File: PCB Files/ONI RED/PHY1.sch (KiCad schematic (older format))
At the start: 40 parts

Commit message: Continued routing work
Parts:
- removed C? (x14): 0.1uF, symbol Device:C_Small
- removed C?: 10uF, symbol Device:CP1_Small
- removed D? (x2): 1N4148, symbol Device:D
- removed J?: JK0654219, Connector_RJ:RJ45_Pulse_JK0654219NL_Horizontal, symbol Connector:JK0654219
- removed R?: 4.7K, symbol Device:R
- removed R? (x2): 10k, symbol Device:R_Small
- removed R?: 220, symbol Device:R_Small
- removed R? (x4): 4.7k, symbol Device:R_Small
- added C43: 10uF, symbol Device:CP1_Small
- added C44, C48, C50, C54, C55: 0.1uF, symbol Device:C_Small
- added C45, C51: 100nF, symbol Device:C_Small
- added C46, C49, C52, C57: 10uF, symbol Device:C_Small
- added C47, C53, C56: 1uF, symbol Device:C_Small
- added D3, D4: 1N4148, symbol Device:D
- added J2: JK0654219, Connector_RJ:RJ45_Pulse_JK0654219NL_Horizontal, symbol Connector:JK0654219
- added R29: 4.7K, symbol Device:R
- added R31, R32, R33, R34: 4.7k, symbol Device:R_Small
- added R35, R39: 10k, symbol Device:R_Small
- added R40: 220, symbol Device:R_Small
- gave numbers to parts that had none: 14
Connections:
- net +3.3V: now also C44.1, C45.1, C46.1, C47.1, C48.1, D4.1 (K), R29.1, R31.2, R32.2, R33.2, R34.1, R35.2, R39.1, R40.2
- net AVDDL: now also C55.1, C56.1, C57.1
- net CLK125: now also R29.2
- net DVDDL: now also C49.1, C50.1, C51.1, C52.1, C53.1, C54.1
- net GND: now also C43.2, C44.2, C45.2, C46.2, C47.2, C48.2, C49.2, C50.2, C51.2, C52.2, C53.2, C54.2, C55.2, C56.2, C57.2
- net M_A: now also J2.10 (MX1-)
- net M_B: now also J2.4 (MX2+)
- net M_C: now also J2.2 (MX3-)
- net M_D: now also J2.9 (MX4-)
- net PHYAD0: now also J2.15 (LED1-), R39.2
- net PHYAD1: now also J2.13 (LED2-)
- net P_A: now also J2.11 (MX1+)
- net P_B: now also J2.5 (MX2-)
- net P_C: now also J2.3 (MX3+)
- net P_D: now also J2.8 (MX4+)
- net RXD1: now also R31.1
- net RXD2: now also R32.1
- net RX_DV: now also R34.2
- net at U9.42 (RESET_N): now also C43.1, D3.2 (A), D4.2 (A), R35.1
- net at C62.1: now also J2.1 (MXCT3)
- net at C60.1: now also J2.12 (MXCT1)
- net at R42.2: now also J2.16 (LED1+)
- net at C61.1: now also J2.6 (MXCT2)
- net at C63.1: now also J2.7 (MXCT4)
- net RX23 renamed RXD3
- net RXD3: now also R33.1
- net TXDO renamed TXD0
- new net: J2.14 (LED2+), R40.1
- new net RESET_N: D3.1 (K)

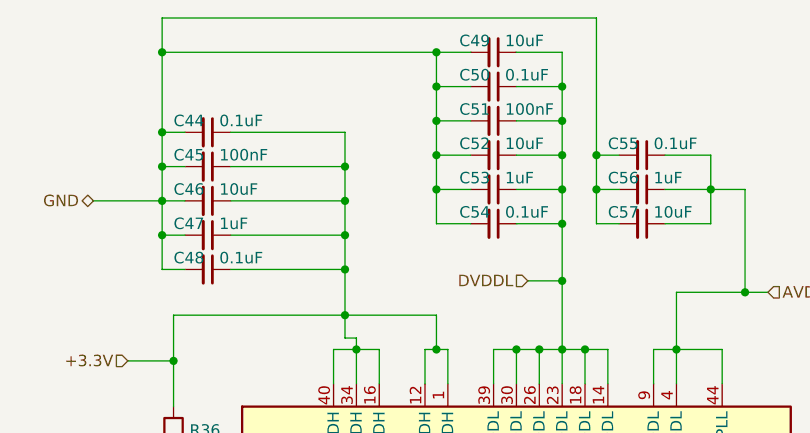
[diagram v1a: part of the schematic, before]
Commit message: Began routing PHY IO
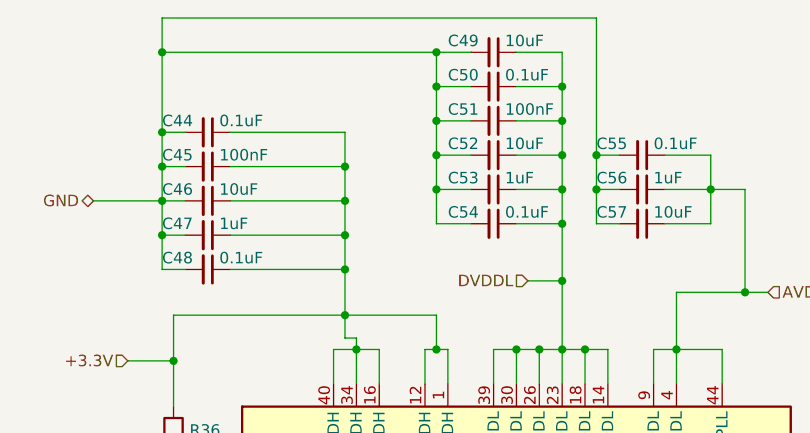
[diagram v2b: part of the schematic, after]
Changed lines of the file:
@@
 $Descr A4 11693 8268
 encoding utf-8
-Sheet 3 5
+Sheet 2 6
 Title ""
 Date ""
@@
 AR Path="/5EE1B380/5EAFA5CA" Ref="C?"  Part="1"
 AR Path="/5EE054E8/5EAFA5CA" Ref="C48"  Part="1"
-F 0 "C48" V 2500 2100 50  0000 L CNN
+F 0 "C48" V 2500 2050 50  0000 L CNN
 F 1 "0.1uF" V 2500 2300 50  0000 L CNN
 F 2 "" H 2550 2250 50  0001 C CNN
@@
 AR Path="/5EE1B380/5EAFA5D0" Ref="C?"  Part="1"
 AR Path="/5EE054E8/5EAFA5D0" Ref="C47"  Part="1"
-F 0 "C47" V 2500 1950 50  0000 L CNN
+F 0 "C47" V 2500 1900 50  0000 L CNN
 F 1 "1uF" V 2500 2150 50  0000 L CNN
 F 2 "" H 2550 2100 50  0001 C CNN
@@
 AR Path="/5EE1B380/5EAFA5D6" Ref="C?"  Part="1"
 AR Path="/5EE054E8/5EAFA5D6" Ref="C46"  Part="1"
-F 0 "C46" V 2500 1800 50  0000 L CNN
+F 0 "C46" V 2500 1750 50  0000 L CNN
 F 1 "10uF" V 2500 2000 50  0000 L CNN
 F 2 "" H 2550 1950 50  0001 C CNN
@@
 AR Path="/5EE1B380/5EAFA5DC" Ref="C?"  Part="1"
 AR Path="/5EE054E8/5EAFA5DC" Ref="C45"  Part="1"
-F 0 "C45" V 2500 1650 50  0000 L CNN
+F 0 "C45" V 2500 1600 50  0000 L CNN
 F 1 "100nF" V 2500 1850 50  0000 L CNN
 F 2 "" H 2550 1800 50  0001 C CNN
@@
 AR Path="/5EE1B380/5EAFA5E2" Ref="C?"  Part="1"
 AR Path="/5EE054E8/5EAFA5E2" Ref="C44"  Part="1"
-F 0 "C44" V 2500 1500 50  0000 L CNN
+F 0 "C44" V 2500 1450 50  0000 L CNN
 F 1 "0.1uF" V 2500 1700 50  0000 L CNN
 F 2 "" H 2550 1650 50  0001 C CNN
@@
 AR Path="/5EE1B380/5EB249C8" Ref="C?"  Part="1"
 AR Path="/5EE054E8/5EB249C8" Ref="C54"  Part="1"
-F 0 "C54" V 3750 1900 50  0000 L CNN
+F 0 "C54" V 3750 1850 50  0000 L CNN
 F 1 "0.1uF" V 3750 2100 50  0000 L CNN
 F 2 "" H 3800 2050 50  0001 C CNN
@@
 AR Path="/5EE1B380/5EB249CE" Ref="C?"  Part="1"
 AR Path="/5EE054E8/5EB249CE" Ref="C53"  Part="1"
-F 0 "C53" V 3750 1750 50  0000 L CNN
+F 0 "C53" V 3750 1700 50  0000 L CNN
 F 1 "1uF" V 3750 1950 50  0000 L CNN
 F 2 "" H 3800 1900 50  0001 C CNN
@@
 AR Path="/5EE1B380/5EB249D4" Ref="C?"  Part="1"
 AR Path="/5EE054E8/5EB249D4" Ref="C52"  Part="1"
-F 0 "C52" V 3750 1600 50  0000 L CNN
+F 0 "C52" V 3750 1550 50  0000 L CNN
 F 1 "10uF" V 3750 1800 50  0000 L CNN
 F 2 "" H 3800 1750 50  0001 C CNN
@@
 AR Path="/5EE1B380/5EB249DA" Ref="C?"  Part="1"
 AR Path="/5EE054E8/5EB249DA" Ref="C51"  Part="1"
-F 0 "C51" V 3750 1450 50  0000 L CNN
+F 0 "C51" V 3750 1400 50  0000 L CNN
 F 1 "100nF" V 3750 1650 50  0000 L CNN
 F 2 "" H 3800 1600 50  0001 C CNN
@@
 AR Path="/5EE1B380/5EB249E0" Ref="C?"  Part="1"
 AR Path="/5EE054E8/5EB249E0" Ref="C50"  Part="1"
-F 0 "C50" V 3750 1300 50  0000 L CNN
+F 0 "C50" V 3750 1250 50  0000 L CNN
 F 1 "0.1uF" V 3750 1500 50  0000 L CNN
 F 2 "" H 3800 1450 50  0001 C CNN
@@
 AR Path="/5EE1B380/5EB249E6" Ref="C?"  Part="1"
 AR Path="/5EE054E8/5EB249E6" Ref="C49"  Part="1"
-F 0 "C49" V 3750 1150 50  0000 L CNN
+F 0 "C49" V 3750 1100 50  0000 L CNN
 F 1 "10uF" V 3750 1350 50  0000 L CNN
 F 2 "" H 3800 1300 50  0001 C CNN
@@
 AR Path="/5EE1B380/5EB4EBAA" Ref="C?"  Part="1"
 AR Path="/5EE054E8/5EB4EBAA" Ref="C57"  Part="1"
-F 0 "C57" V 4400 1900 50  0000 L CNN
+F 0 "C57" V 4400 1850 50  0000 L CNN
 F 1 "10uF" V 4400 2100 50  0000 L CNN
 F 2 "" H 4450 2050 50  0001 C CNN
@@
 AR Path="/5EE1B380/5EB4EBB0" Ref="C?"  Part="1"
 AR Path="/5EE054E8/5EB4EBB0" Ref="C56"  Part="1"
-F 0 "C56" V 4400 1750 50  0000 L CNN
+F 0 "C56" V 4400 1700 50  0000 L CNN
 F 1 "1uF" V 4400 1950 50  0000 L CNN
 F 2 "" H 4450 1900 50  0001 C CNN
@@
 AR Path="/5EE1B380/5EB4EBB6" Ref="C?"  Part="1"
 AR Path="/5EE054E8/5EB4EBB6" Ref="C55"  Part="1"
-F 0 "C55" V 4400 1600 50  0000 L CNN
+F 0 "C55" V 4400 1550 50  0000 L CNN
 F 1 "0.1uF" V 4400 1800 50  0000 L CNN
 F 2 "" H 4450 1750 50  0001 C CNN

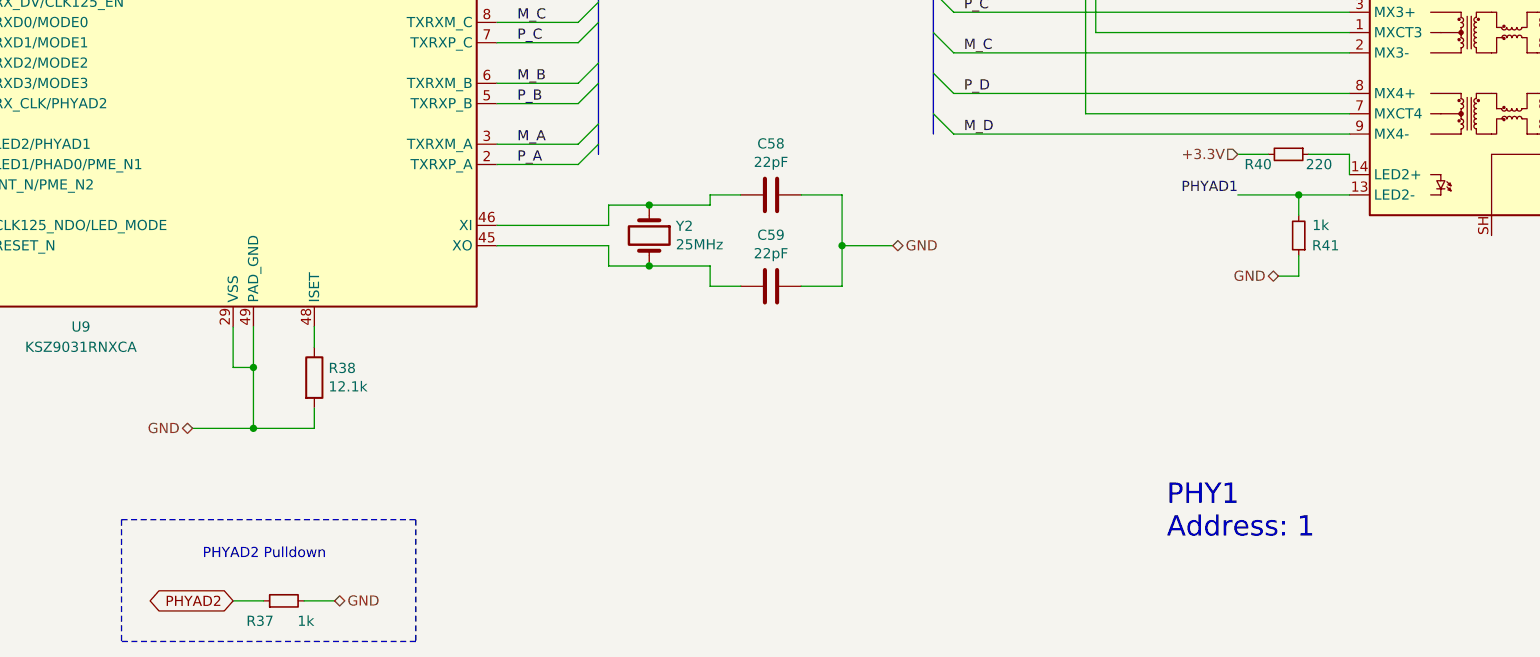
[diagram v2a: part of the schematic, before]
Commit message: Added extra PHYs and expanded IO
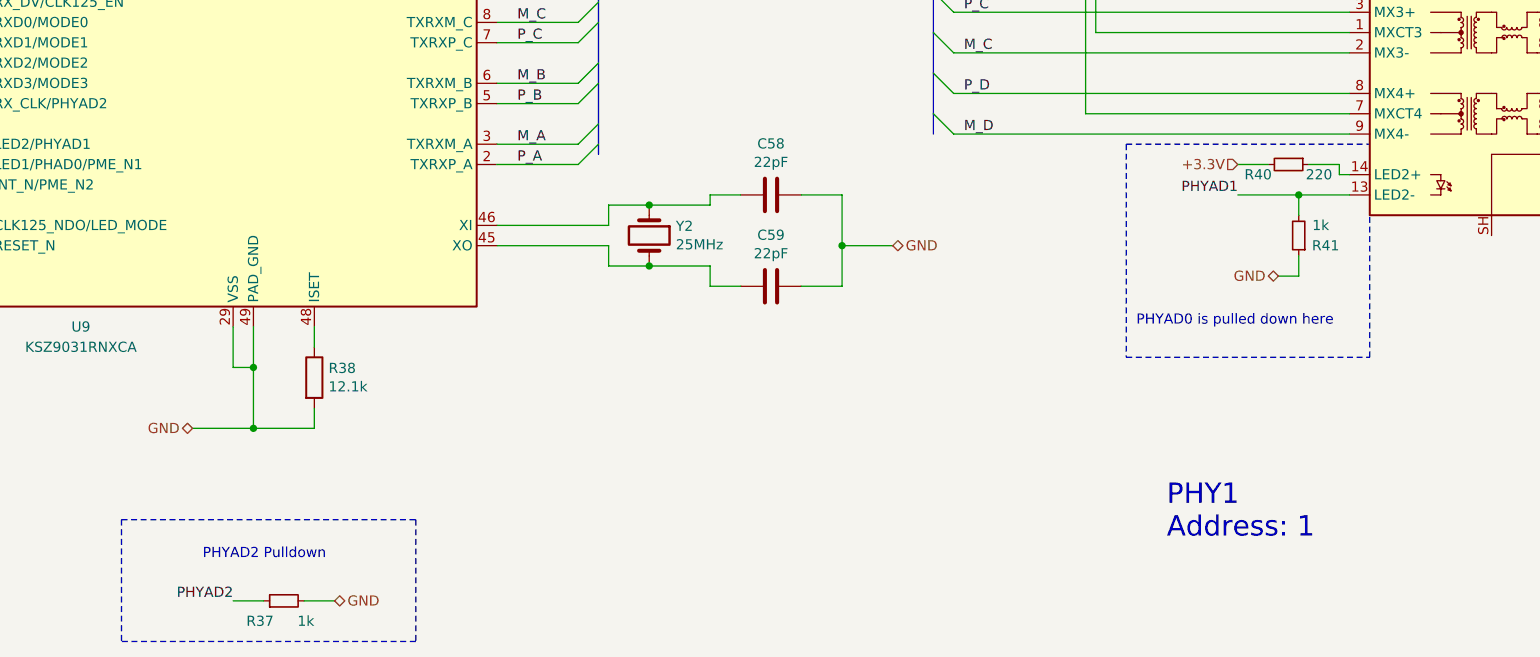
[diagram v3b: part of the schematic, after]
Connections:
- net PHYAD2 renamed RX_CLK
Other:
- note added: "PHYAD0 is pulled down here"
- moved on the sheet: R40
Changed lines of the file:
@@
 $Descr A4 11693 8268
 encoding utf-8
-Sheet 2 6
+Sheet 2 8
 Title ""
 Date ""
@@
 	1    0    0    -1
 $EndComp
-Text HLabel 8850 5100 0    50   Input ~ 0
+Text HLabel 8850 5150 0    50   Input ~ 0
 +3.3V
 $Comp
 L Device:R_Small R40
 U 1 1 5EBFAB14
-P 9100 5100
-F 0 "R40" V 9150 4950 50  0000 C CNN
-F 1 "220" V 9150 5250 50  0000 C CNN
-F 2 "" H 9100 5100 50  0001 C CNN
-F 3 "~" H 9100 5100 50  0001 C CNN
-	1    9100 5100
-	0    1    1    0
-$EndComp
-Wire Wire Line
-	8850 5100 9000 5100
-Wire Wire Line
-	9200 5100 9400 5100
-Wire Wire Line
-	9400 5100 9400 5200
+P 9100 5150
+F 0 "R40" V 9150 5000 50  0000 C CNN
+F 1 "220" V 9150 5300 50  0000 C CNN
+F 2 "" H 9100 5150 50  0001 C CNN
+F 3 "~" H 9100 5150 50  0001 C CNN
+	1    9100 5150
+	0    1    1    0
+$EndComp
+Wire Wire Line
+	8850 5150 9000 5150
 $Comp
 L Device:R_Small R41
@@
 Text Notes 8500 7000 0    100  ~ 0
 PHY1\nAddress: 1
-Text GLabel 3900 7300 0    50   BiDi ~ 0
-PHYAD2
 $Comp
 L Device:R_Small R?
@@
 Text HLabel 2250 3450 0    50   Input ~ 0
 MDIO
+Text Label 3900 7300 2    50   ~ 0
+PHYAD2
+Wire Notes Line
+	8300 5050 8300 6100
+Wire Notes Line
+	9500 6100 9500 5400
+Text Notes 8350 5950 0    50   ~ 0
+PHYAD0 is pulled down here
+Wire Notes Line
+	8300 6100 9500 6100
+Wire Notes Line
+	8300 5050 9500 5050
+Wire Wire Line
+	9200 5150 9350 5150
+Wire Wire Line
+	9350 5150 9350 5200
+Wire Wire Line
+	9350 5200 9400 5200
 Wire Bus Line
 	7350 3500 7350 5000
